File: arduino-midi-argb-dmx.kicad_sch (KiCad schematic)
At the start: 26 parts

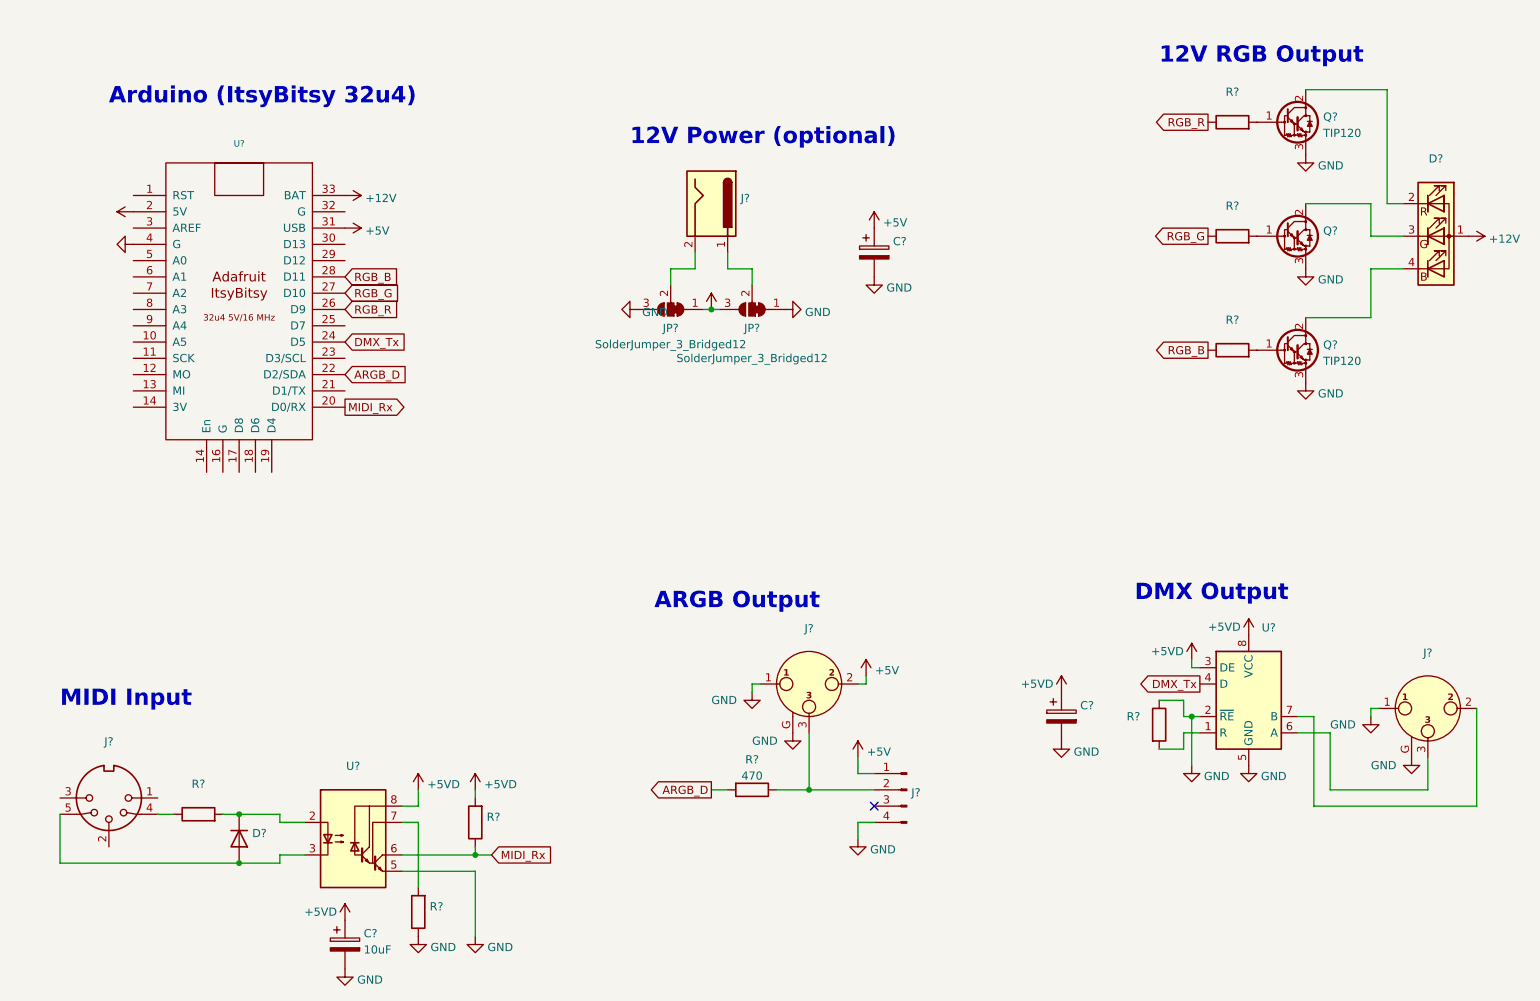
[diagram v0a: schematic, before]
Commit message: Revision 1 of PCB. Provided support for 5V or 12V analog LED strips.
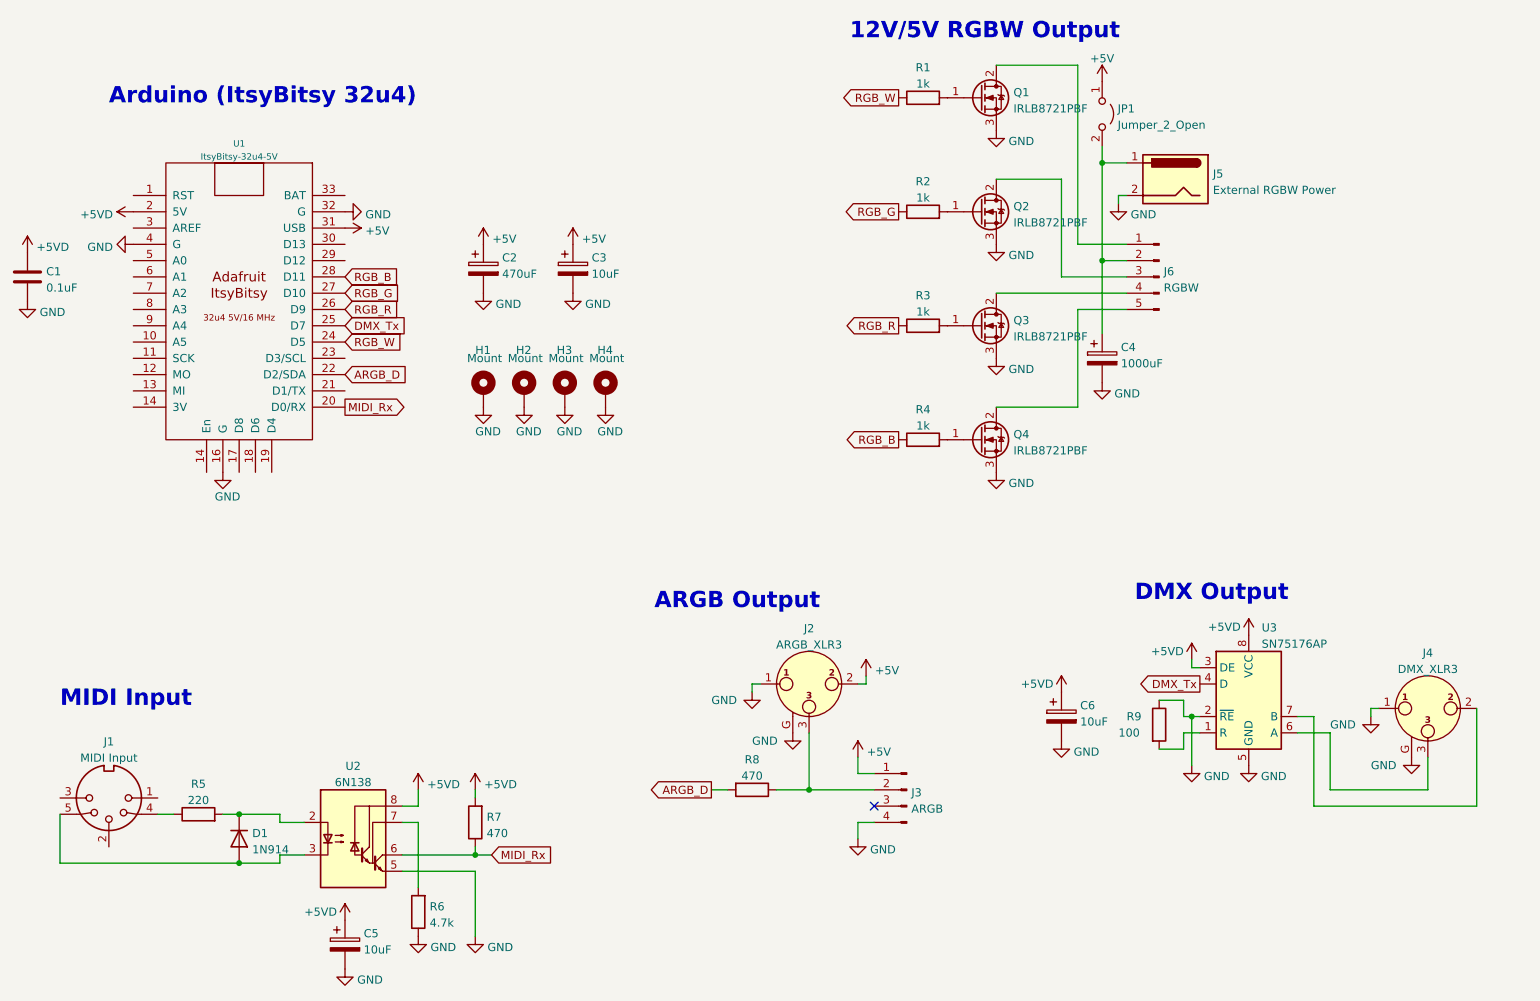
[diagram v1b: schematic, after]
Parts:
- removed D?: (no value), symbol Device:LED_ARGB
- removed J?: (no value), symbol Connector:Barrel_Jack
- removed JP? (x2): SolderJumper_3_Bridged12, symbol Jumper:SolderJumper_3_Bridged12
- removed Q?: (no value), symbol Transistor_BJT:TIP120
- removed Q? (x2): TIP120, Package_TO_SOT_THT:TO-220-3_Vertical, symbol Transistor_BJT:TIP120
- added C1: 0.1uF, Capacitor_THT:C_Rect_L4.0mm_W2.5mm_P2.50mm, symbol Device:C
- added C2: 470uF, Capacitor_THT:CP_Axial_L20.0mm_D10.0mm_P26.00mm_Horizontal, symbol Device:C_Polarized
- added C3: 10uF, Capacitor_THT:CP_Radial_D5.0mm_P2.50mm, symbol Device:C_Polarized
- added H1, H2, H3, H4: Mount, MountingHole:MountingHole_3.2mm_M3_Pad, symbol Mechanical:MountingHole_Pad
- added J5: External RGBW Power, Connector_BarrelJack:BarrelJack_Horizontal, symbol Connector:Barrel_Jack
- added J6: RGBW, Connector_PinHeader_2.54mm:PinHeader_1x05_P2.54mm_Horizontal, symbol Connector:Conn_01x05_Male
- added JP1: Jumper_2_Open, Connector_PinHeader_2.54mm:PinHeader_1x02_P2.54mm_Vertical, symbol Jumper:Jumper_2_Open
- added Q1, Q2, Q3, Q4: IRLB8721PBF, Package_TO_SOT_THT:TO-220-3_Vertical, symbol Transistor_FET:IRLB8721PBF
- added R4: 1k, Resistor_THT:R_Axial_DIN0207_L6.3mm_D2.5mm_P7.62mm_Horizontal, symbol Device:R
- C4: renamed from C?; value (none) -> 1000uF; footprint (none) -> Capacitor_THT:CP_Axial_L20.0mm_D10.0mm_P26.00mm_Horizontal
- C5: renamed from C?; footprint (none) -> Capacitor_THT:CP_Radial_D5.0mm_P2.50mm
- C6: renamed from C?; value (none) -> 10uF; footprint (none) -> Capacitor_THT:CP_Radial_D5.0mm_P2.50mm
- D1: renamed from D?; value (none) -> 1N914; footprint (none) -> Diode_THT:D_DO-35_SOD27_P7.62mm_Horizontal
- J1: renamed from J?; value (none) -> MIDI Input; footprint (none) -> w_conn_av:din-5
- J2: renamed from J?; value (none) -> ARGB_XLR3; footprint (none) -> Connector_Audio:Jack_XLR_Neutrik_NC3FAAH2_Horizontal
- J3: renamed from J?; value (none) -> ARGB; footprint (none) -> Connector_PinHeader_2.54mm:PinHeader_1x04_P2.54mm_Horizontal
- J4: renamed from J?; value (none) -> DMX_XLR3; footprint (none) -> Connector_Audio:Jack_XLR_Neutrik_NC3FAAH2_Horizontal
- R1, R2, R3: renamed from R?; value (none) -> 1k; footprint (none) -> Resistor_THT:R_Axial_DIN0207_L6.3mm_D2.5mm_P7.62mm_Horizontal
- R5: renamed from R?; value (none) -> 220; footprint (none) -> Resistor_THT:R_Axial_DIN0207_L6.3mm_D2.5mm_P7.62mm_Horizontal
- R6: renamed from R?; value (none) -> 4.7k; footprint (none) -> Resistor_THT:R_Axial_DIN0207_L6.3mm_D2.5mm_P7.62mm_Horizontal
- R7: renamed from R?; value (none) -> 470; footprint (none) -> Resistor_THT:R_Axial_DIN0207_L6.3mm_D2.5mm_P7.62mm_Horizontal
- R8: renamed from R?; footprint (none) -> Resistor_THT:R_Axial_DIN0207_L6.3mm_D2.5mm_P7.62mm_Horizontal
- R9: renamed from R?; value (none) -> 100; footprint (none) -> Resistor_THT:R_Axial_DIN0207_L6.3mm_D2.5mm_P7.62mm_Horizontal
- U1: renamed from U?; value (none) -> ItsyBitsy-32u4-5V; footprint (none) -> itsybitsy-32u4-5v:ItsyBitsy_32u4
- U2: renamed from U?; value (none) -> 6N138; footprint (none) -> Package_DIP:DIP-8_W7.62mm_Socket_LongPads
- U3: renamed from U?; value (none) -> SN75176AP; footprint (none) -> Package_DIP:DIP-8_W7.62mm_Socket_LongPads
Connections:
- net +5V: now also C2.1, C3.1, JP1.1 (A); no longer C4.1
- net +5VD: now also C1.1
- net DMX_Tx: now also U1.25 (D7); no longer U1.24 (D5)
- net GND: now also U1.16 (G), U1.32 (G), C1.2, C2.2, C3.2, H1.1, H2.1, H3.1, H4.1, J5.2, Q1.3 (S), Q2.3 (S), Q3.3 (S), Q4.3 (S)
- net RGB_B: now also R4.1; no longer R3.1
- net RGB_R: now also R3.1; no longer R1.1
- net at R1.2: now also Q1.1 (G)
- net at R2.2: now also Q2.1 (G)
- net at R3.2: now also Q3.1 (G)
- net +12V: no longer names the net of U1.33 (BAT)
- new net: J6.4 (Pin_4), Q3.2 (D)
- new net: Q4.1 (G), R4.2
- new net: C4.1, J5.1, J6.2 (Pin_2), JP1.2 (B)
- new net: J6.3 (Pin_3), Q2.2 (D)
- new net: J6.1 (Pin_1), Q1.2 (D)
- new net: J6.5 (Pin_5), Q4.2 (D)
- new net RGB_W: R1.1, U1.24 (D5)
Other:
- note added: "12V/5V RGBW Output"
- note removed: "12V Power (optional)"
- note removed: "12V RGB Output"
- moved on the sheet: C4, R1, R2, R3
